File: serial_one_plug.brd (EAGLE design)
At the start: 14.3 x 17.8 mm, 3 parts

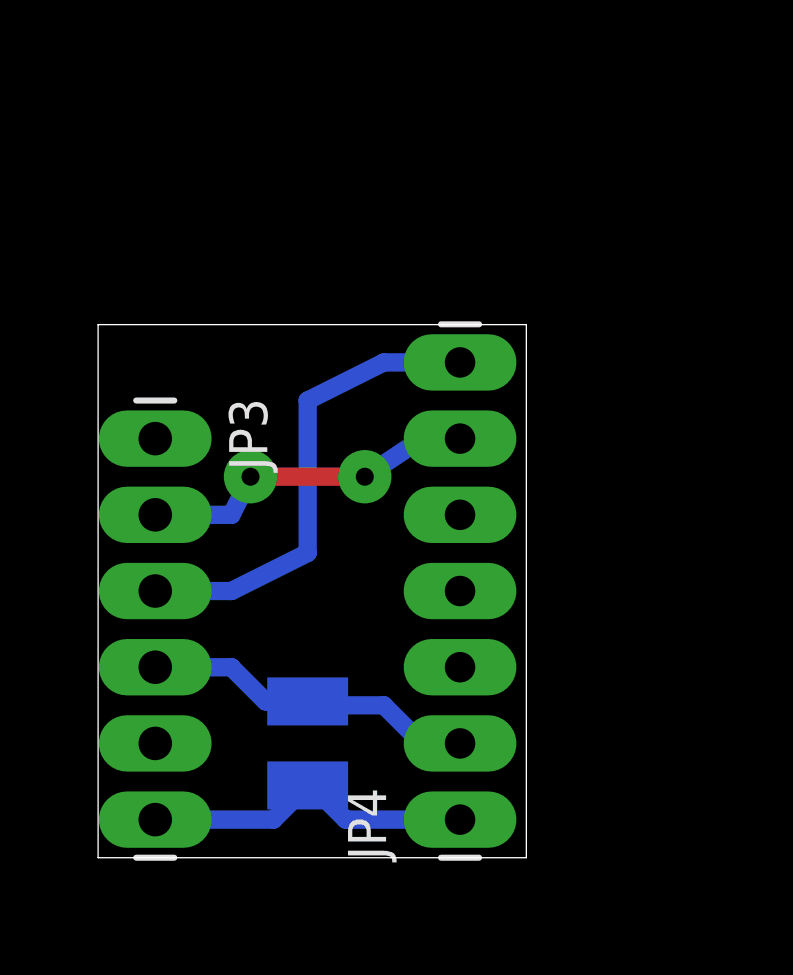
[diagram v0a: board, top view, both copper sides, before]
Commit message: serial plug version 2 -- reset + prog
added more (more more!) functionality to the serial plug
has a ground jumper for PD2, pushbutton on reset
enabling it to work with bootloader
printed out, run, it's great.
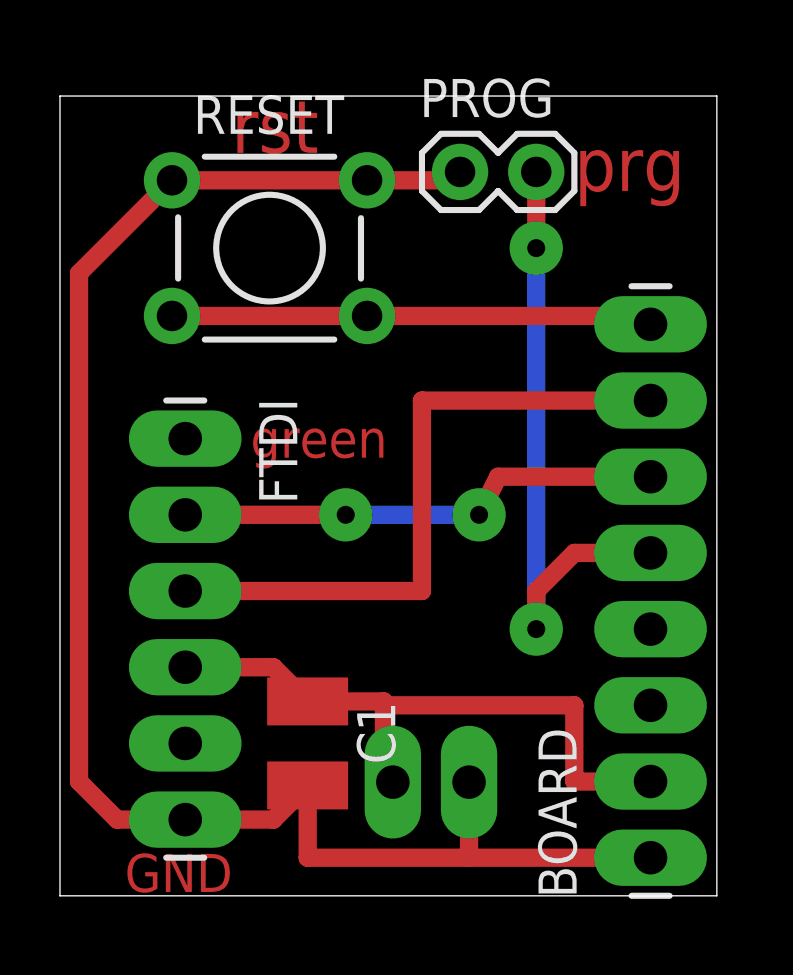
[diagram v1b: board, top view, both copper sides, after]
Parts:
- removed JP3: (no value), SparkFun-Connectors:1X06_LONGPADS
- removed JP4: (no value), SparkFun-Connectors:1X07_LONGPADS
- added BOARD: (no value), SparkFun-Connectors:1X08_LONGPADS
- added FTDI: (no value), SparkFun-Connectors:1X06_LONGPADS
- added POWER_RAIL: M02PTH3, SparkFun-Connectors:1X02_LONGPADS
- added PROG: M02PTH, SparkFun-Connectors:1X02
- added RESET: (no value), SparkFun-Electromechanical:TACTILE-PTH
- flipped C1 to the top
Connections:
- new net PD2: BOARD.5, PROG.2
- new net RESET: BOARD.8, RESET.3, RESET.4
- net GND: now also BOARD.1, FTDI.6, POWER_RAIL.1, PROG.1, RESET.1, RESET.2; no longer JP3.6, JP4.1
- net RX: now also BOARD.6, FTDI.2; no longer JP3.2, JP4.6
- net TX: now also BOARD.7, FTDI.3; no longer JP3.3, JP4.7
- net VCC: now also BOARD.2, FTDI.4, POWER_RAIL.2; no longer JP3.4, JP4.2
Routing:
- net GND: track 11.1 -> 56.0 mm
- net PD2: track 0.00 -> 20.8 mm, vias 0 -> 2
- net RESET: track 0.00 -> 16.1 mm
- net VCC: track 11.2 -> 21.5 mm
- net TX: track 15.8 -> 21.9 mm
- net RX: track 11.3 -> 16.3 mm
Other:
- board size 14.3 x 17.8 mm -> 21.9 x 26.7 mm
- board text added: "GND"
- board text added: "green"
- board text added: "prg"
- board text added: "rst"
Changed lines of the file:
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@@
 <setting verticaltext="up"/>
 </settings>
-<grid distance="0.05" unitdist="inch" unit="inch" style="lines" multiple="1" display="yes" altdistance="0.025" altunitdist="inch" altunit="inch"/>
+<grid distance="0.05" unitdist="inch" unit="inch" style="lines" multiple="2" display="yes" altdistance="0.01" altunitdist="inch" altunit="inch"/>
 <layers>
 <layer number="1" name="Top" color="4" fill="1" visible="yes" active="yes"/>
@@
 <board>
 <plain>
-<wire x1="-0.635" y1="0" x2="13.64" y2="0" width="0" layer="20"/>
-<wire x1="13.64" y1="0" x2="13.64" y2="17.77" width="0" layer="20"/>
-<wire x1="13.64" y1="17.77" x2="-0.635" y2="17.77" width="0" layer="20"/>
-<wire x1="-0.635" y1="17.77" x2="-0.635" y2="0" width="0" layer="20"/>
+<wire x1="-1.905" y1="-1.27" x2="19.99" y2="-1.27" width="0" layer="20"/>
+<wire x1="19.99" y1="-1.27" x2="19.99" y2="25.39" width="0" layer="20"/>
+<wire x1="19.99" y1="25.39" x2="-1.905" y2="25.39" width="0" layer="20"/>
+<wire x1="-1.905" y1="25.39" x2="-1.905" y2="-1.27" width="0" layer="20"/>
+<text x="15.24" y="22.225" size="1.778" layer="1">prg</text>
+<text x="3.81" y="23.495" size="1.778" layer="1">rst</text>
+<text x="4.445" y="13.335" size="1.27" layer="1">green</text>
+<text x="0.254" y="-1.143" size="1.27" layer="1">GND</text>
 </plain>
 <attributes>
@@
 </autorouter>
 <elements>
-<element name="C1" library="resistor" package="C1210" value="" x="6.35" y="3.81" rot="MR270"/>
-<element name="JP3" library="SparkFun-Connectors" package="1X06_LONGPADS" value="" x="1.27" y="13.97" rot="R270"/>
-<element name="JP4" library="SparkFun-Connectors" package="1X07_LONGPADS" value="" x="11.43" y="1.27" rot="R90"/>
+<element name="C1" library="resistor" package="C1210" value="" x="6.35" y="3.81" rot="R270"/>
+<element name="FTDI" library="SparkFun-Connectors" package="1X06_LONGPADS" value="" x="2.27" y="13.97" rot="R270"/>
+<element name="POWER_RAIL" library="SparkFun-Connectors" package="1X02_LONGPADS" value="M02PTH3" x="11.73" y="2.52" rot="R180"/>
+<element name="BOARD" library="SparkFun-Connectors" package="1X08_LONGPADS" value="" x="17.78" y="0" rot="R90"/>
+<element name="RESET" library="SparkFun-Electromechanical" package="TACTILE-PTH" value="" x="5.08" y="20.32"/>
+<element name="PROG" library="SparkFun-Connectors" package="1X02" value="M02PTH" x="11.43" y="22.86"/>
 </elements>
 <signals>
 <signal name="GND">
 <contactref element="C1" pad="2"/>
-<wire x1="6.35" y1="2.41" x2="6.48" y2="2.41" width="0.6096" layer="16"/>
-<wire x1="6.48" y1="2.41" x2="7.62" y2="1.27" width="0.6096" layer="16"/>
-<contactref element="JP3" pad="6"/>
-<contactref element="JP4" pad="1"/>
-<wire x1="1.27" y1="1.27" x2="5.21" y2="1.27" width="0.6096" layer="16"/>
-<wire x1="5.21" y1="1.27" x2="6.35" y2="2.41" width="0.6096" layer="16"/>
-<wire x1="7.62" y1="1.27" x2="11.43" y2="1.27" width="0.6096" layer="16"/>
+<contactref element="FTDI" pad="6"/>
+<contactref element="POWER_RAIL" pad="1"/>
+<wire x1="2.27" y1="1.27" x2="5.21" y2="1.27" width="0.6096" layer="1"/>
+<wire x1="5.21" y1="1.27" x2="6.35" y2="2.41" width="0.6096" layer="1"/>
+<contactref element="BOARD" pad="1"/>
+<wire x1="17.78" y1="0" x2="11.73" y2="0" width="0.6096" layer="1"/>
+<wire x1="11.73" y1="0" x2="11.73" y2="2.52" width="0.6096" layer="1"/>
+<wire x1="6.35" y1="2.41" x2="6.35" y2="0" width="0.6096" layer="1"/>
+<wire x1="6.35" y1="0" x2="11.73" y2="0" width="0.6096" layer="1"/>
+<contactref element="RESET" pad="1"/>
+<contactref element="RESET" pad="2"/>
+<contactref element="PROG" pad="1"/>
+<wire x1="2.27" y1="1.27" x2="0" y2="1.27" width="0.6096" layer="1"/>
+<wire x1="0" y1="1.27" x2="-1.27" y2="2.54" width="0.6096" layer="1"/>
+<wire x1="-1.27" y1="2.54" x2="-1.27" y2="19.4818" width="0.6096" layer="1"/>
+<wire x1="-1.27" y1="19.4818" x2="1.8288" y2="22.5806" width="0.6096" layer="1"/>
+<wire x1="1.8288" y1="22.5806" x2="8.3312" y2="22.5806" width="0.6096" layer="1"/>
+<wire x1="8.3312" y1="22.5806" x2="11.1506" y2="22.5806" width="0.6096" layer="1"/>
+<wire x1="11.1506" y1="22.5806" x2="11.43" y2="22.86" width="0.6096" layer="1"/>
 </signal>
 <signal name="VCC">
 <contactref element="C1" pad="1"/>
-<contactref element="JP3" pad="4"/>
-<contactref element="JP4" pad="2"/>
-<wire x1="11.43" y1="3.81" x2="10.16" y2="3.81" width="0.6096" layer="16"/>
-<wire x1="10.16" y1="3.81" x2="8.89" y2="5.08" width="0.6096" layer="16"/>
-<wire x1="8.89" y1="5.08" x2="6.48" y2="5.08" width="0.6096" layer="16"/>
-<wire x1="6.48" y1="5.08" x2="6.35" y2="5.21" width="0.6096" layer="16"/>
-<wire x1="6.35" y1="5.21" x2="4.95" y2="5.21" width="0.6096" layer="16"/>
-<wire x1="4.95" y1="5.21" x2="3.81" y2="6.35" width="0.6096" layer="16"/>
-<wire x1="3.81" y1="6.35" x2="1.27" y2="6.35" width="0.6096" layer="16"/>
+<contactref element="FTDI" pad="4"/>
+<contactref element="POWER_RAIL" pad="2"/>
+<wire x1="2.27" y1="6.35" x2="5.21" y2="6.35" width="0.6096" layer="1"/>
+<wire x1="5.21" y1="6.35" x2="6.35" y2="5.21" width="0.6096" layer="1"/>
+<contactref element="BOARD" pad="2"/>
+<wire x1="6.35" y1="5.21" x2="8.89" y2="5.21" width="0.6096" layer="1"/>
+<wire x1="8.89" y1="5.08" x2="8.89" y2="3.81" width="0.6096" layer="1"/>
+<wire x1="8.89" y1="3.81" x2="9.19" y2="3.81" width="0.6096" layer="1"/>
+<wire x1="9.19" y1="3.81" x2="9.19" y2="2.52" width="0.6096" layer="1"/>
+<wire x1="17.78" y1="2.54" x2="15.24" y2="2.54" width="0.6096" layer="1"/>
+<wire x1="15.24" y1="2.54" x2="15.24" y2="5.08" width="0.6096" layer="1"/>
+<wire x1="15.24" y1="5.08" x2="8.89" y2="5.08" width="0.6096" layer="1"/>
+<wire x1="8.89" y1="5.08" x2="8.89" y2="5.21" width="0.6096" layer="1"/>
 </signal>
 <signal name="TX">
-<contactref element="JP3" pad="3"/>
-<contactref element="JP4" pad="7"/>
-<wire x1="1.27" y1="8.89" x2="3.81" y2="8.89" width="0.6096" layer="16"/>
-<wire x1="3.81" y1="8.89" x2="6.35" y2="10.16" width="0.6096" layer="16"/>
-<wire x1="6.35" y1="10.16" x2="6.35" y2="15.24" width="0.6096" layer="16"/>
-<wire x1="6.35" y1="15.24" x2="8.89" y2="16.51" width="0.6096" layer="16"/>
-<wire x1="8.89" y1="16.51" x2="11.43" y2="16.51" width="0.6096" layer="16"/>
+<contactref element="FTDI" pad="3"/>
+<contactref element="BOARD" pad="7"/>
+<wire x1="2.27" y1="8.89" x2="10.16" y2="8.89" width="0.6096" layer="1"/>
+<wire x1="10.16" y1="8.89" x2="10.16" y2="15.24" width="0.6096" layer="1"/>
+<wire x1="10.16" y1="15.24" x2="17.78" y2="15.24" width="0.6096" layer="1"/>
 </signal>
 <signal name="RX">
-<contactref element="JP3" pad="2"/>
-<contactref element="JP4" pad="6"/>
-<wire x1="1.27" y1="11.43" x2="3.81" y2="11.43" width="0.6096" layer="16"/>
-<wire x1="3.81" y1="11.43" x2="4.445" y2="12.7" width="0.6096" layer="16"/>
-<via x="4.445" y="12.7" extent="1-16" drill="0.6" diameter="1.778" shape="octagon"/>
-<wire x1="4.445" y1="12.7" x2="8.255" y2="12.7" width="0.6096" layer="1"/>
-<via x="8.255" y="12.7" extent="1-16" drill="0.6" diameter="1.778" shape="octagon"/>
-<wire x1="8.255" y1="12.7" x2="10.16" y2="13.97" width="0.6096" layer="16"/>
-<wire x1="10.16" y1="13.97" x2="11.43" y2="13.97" width="0.6096" layer="16"/>
+<contactref element="FTDI" pad="2"/>
+<contactref element="BOARD" pad="6"/>
+<wire x1="2.27" y1="11.43" x2="7.62" y2="11.43" width="0.6096" layer="1"/>
+<via x="7.62" y="11.43" extent="1-16" drill="0.6" diameter="1.778" shape="octagon"/>
+<wire x1="7.62" y1="11.43" x2="12.065" y2="11.43" width="0.6096" layer="16"/>
+<via x="12.065" y="11.43" extent="1-16" drill="0.6" diameter="1.778" shape="octagon"/>
+<wire x1="12.065" y1="11.43" x2="12.7" y2="12.7" width="0.6096" layer="1"/>
+<wire x1="12.7" y1="12.7" x2="17.78" y2="12.7" width="0.6096" layer="1"/>
+</signal>
+<signal name="RESET">
+<contactref element="RESET" pad="4"/>
+<contactref element="RESET" pad="3"/>
+<contactref element="BOARD" pad="8"/>
+<wire x1="1.8288" y1="18.0594" x2="8.3312" y2="18.0594" width="0.6096" layer="1"/>
+<wire x1="8.3312" y1="18.0594" x2="17.5006" y2="18.0594" width="0.6096" layer="1"/>
+<wire x1="17.5006" y1="18.0594" x2="17.78" y2="17.78" width="0.6096" layer="1"/>
+</signal>
+<signal name="PD2">
+<contactref element="BOARD" pad="5"/>
+<contactref element="PROG" pad="2"/>
+<wire x1="13.97" y1="22.86" x2="13.97" y2="20.32" width="0.6096" layer="1"/>
+<via x="13.97" y="20.32" extent="1-16" drill="0.6" diameter="1.778" shape="octagon"/>
+<wire x1="13.97" y1="20.32" x2="13.97" y2="7.62" width="0.6096" layer="16"/>
+<via x="13.97" y="7.62" extent="1-16" drill="0.6" diameter="1.778" shape="octagon"/>
+<wire x1="13.97" y1="7.62" x2="13.97" y2="8.89" width="0.6096" layer="1"/>
+<wire x1="13.97" y1="8.89" x2="15.24" y2="10.16" width="0.6096" layer="1"/>
+<wire x1="15.24" y1="10.16" x2="17.78" y2="10.16" width="0.6096" layer="1"/>
 </signal>
 </signals>

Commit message: shrunk cap on serial board to 1206 from 1210
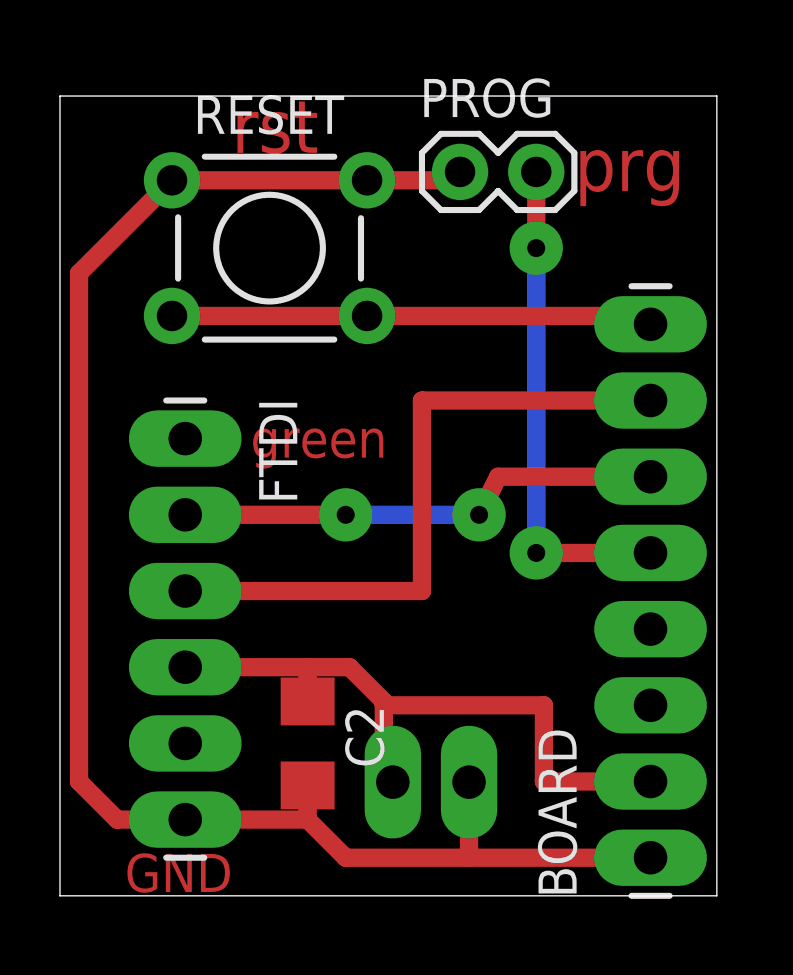
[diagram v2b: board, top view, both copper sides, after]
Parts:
- removed C1: (no value), resistor:C1210
- added C2: 0.1 uF, rcl:C1206
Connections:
- net GND: now also C2.2; no longer C1.2
- net VCC: now also C2.1; no longer C1.1
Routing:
- net PD2: track 20.8 -> 16.5 mm
- net GND: track 56.0 -> 54.8 mm
- net VCC: track 21.5 -> 22.7 mm
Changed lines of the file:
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@@
 </autorouter>
 <elements>
-<element name="C1" library="resistor" package="C1210" value="" x="6.35" y="3.81" rot="R270"/>
 <element name="FTDI" library="SparkFun-Connectors" package="1X06_LONGPADS" value="" x="2.27" y="13.97" rot="R270"/>
 <element name="POWER_RAIL" library="SparkFun-Connectors" package="1X02_LONGPADS" value="M02PTH3" x="11.73" y="2.52" rot="R180"/>
@@
 <element name="RESET" library="SparkFun-Electromechanical" package="TACTILE-PTH" value="" x="5.08" y="20.32"/>
 <element name="PROG" library="SparkFun-Connectors" package="1X02" value="M02PTH" x="11.43" y="22.86"/>
+<element name="C2" library="rcl" package="C1206" value="0.1 uF" x="6.35" y="3.81" rot="R270"/>
 </elements>
 <signals>
 <signal name="GND">
-<contactref element="C1" pad="2"/>
 <contactref element="FTDI" pad="6"/>
 <contactref element="POWER_RAIL" pad="1"/>
-<wire x1="2.27" y1="1.27" x2="5.21" y2="1.27" width="0.6096" layer="1"/>
-<wire x1="5.21" y1="1.27" x2="6.35" y2="2.41" width="0.6096" layer="1"/>
+<wire x1="2.27" y1="1.27" x2="6.35" y2="1.27" width="0.6096" layer="1"/>
 <contactref element="BOARD" pad="1"/>
 <wire x1="17.78" y1="0" x2="11.73" y2="0" width="0.6096" layer="1"/>
 <wire x1="11.73" y1="0" x2="11.73" y2="2.52" width="0.6096" layer="1"/>
-<wire x1="6.35" y1="2.41" x2="6.35" y2="0" width="0.6096" layer="1"/>
-<wire x1="6.35" y1="0" x2="11.73" y2="0" width="0.6096" layer="1"/>
 <contactref element="RESET" pad="1"/>
 <contactref element="RESET" pad="2"/>
@@
 <wire x1="8.3312" y1="22.5806" x2="11.1506" y2="22.5806" width="0.6096" layer="1"/>
 <wire x1="11.1506" y1="22.5806" x2="11.43" y2="22.86" width="0.6096" layer="1"/>
+<contactref element="C2" pad="2"/>
+<wire x1="11.73" y1="0" x2="7.62" y2="0" width="0.6096" layer="1"/>
+<wire x1="7.62" y1="0" x2="6.35" y2="1.27" width="0.6096" layer="1"/>
+<wire x1="6.35" y1="1.27" x2="6.35" y2="2.41" width="0.6096" layer="1"/>
 </signal>
 <signal name="VCC">
-<contactref element="C1" pad="1"/>
 <contactref element="FTDI" pad="4"/>
 <contactref element="POWER_RAIL" pad="2"/>
-<wire x1="2.27" y1="6.35" x2="5.21" y2="6.35" width="0.6096" layer="1"/>
-<wire x1="5.21" y1="6.35" x2="6.35" y2="5.21" width="0.6096" layer="1"/>
+<wire x1="2.27" y1="6.35" x2="6.35" y2="6.35" width="0.6096" layer="1"/>
 <contactref element="BOARD" pad="2"/>
-<wire x1="6.35" y1="5.21" x2="8.89" y2="5.21" width="0.6096" layer="1"/>
+<wire x1="6.35" y1="6.35" x2="7.75" y2="6.35" width="0.6096" layer="1"/>
 <wire x1="8.89" y1="5.08" x2="8.89" y2="3.81" width="0.6096" layer="1"/>
 <wire x1="8.89" y1="3.81" x2="9.19" y2="3.81" width="0.6096" layer="1"/>
 <wire x1="9.19" y1="3.81" x2="9.19" y2="2.52" width="0.6096" layer="1"/>
-<wire x1="17.78" y1="2.54" x2="15.24" y2="2.54" width="0.6096" layer="1"/>
-<wire x1="15.24" y1="2.54" x2="15.24" y2="5.08" width="0.6096" layer="1"/>
-<wire x1="15.24" y1="5.08" x2="8.89" y2="5.08" width="0.6096" layer="1"/>
+<wire x1="17.78" y1="2.54" x2="14.224" y2="2.54" width="0.6096" layer="1"/>
+<wire x1="14.224" y1="2.54" x2="14.224" y2="5.08" width="0.6096" layer="1"/>
+<wire x1="14.224" y1="5.08" x2="8.89" y2="5.08" width="0.6096" layer="1"/>
 <wire x1="8.89" y1="5.08" x2="8.89" y2="5.21" width="0.6096" layer="1"/>
+<contactref element="C2" pad="1"/>
+<wire x1="7.75" y1="6.35" x2="8.89" y2="5.21" width="0.6096" layer="1"/>
+<wire x1="6.35" y1="5.21" x2="6.35" y2="6.35" width="0.6096" layer="1"/>
 </signal>
 <signal name="TX">
@@
 <wire x1="13.97" y1="22.86" x2="13.97" y2="20.32" width="0.6096" layer="1"/>
 <via x="13.97" y="20.32" extent="1-16" drill="0.6" diameter="1.778" shape="octagon"/>
-<wire x1="13.97" y1="20.32" x2="13.97" y2="7.62" width="0.6096" layer="16"/>
-<via x="13.97" y="7.62" extent="1-16" drill="0.6" diameter="1.778" shape="octagon"/>
-<wire x1="13.97" y1="7.62" x2="13.97" y2="8.89" width="0.6096" layer="1"/>
-<wire x1="13.97" y1="8.89" x2="15.24" y2="10.16" width="0.6096" layer="1"/>
-<wire x1="15.24" y1="10.16" x2="17.78" y2="10.16" width="0.6096" layer="1"/>
+<wire x1="13.97" y1="20.32" x2="13.97" y2="10.16" width="0.6096" layer="16"/>
+<via x="13.97" y="10.16" extent="1-16" drill="0.6" diameter="1.778" shape="octagon"/>
+<wire x1="13.97" y1="10.16" x2="17.78" y2="10.16" width="0.6096" layer="1"/>
 </signal>
 </signals>
